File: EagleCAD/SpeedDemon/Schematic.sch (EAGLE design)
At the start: 45 parts, among them Q1 DMC2700, U1 LM3676, U3 STM32F072-LQFP48

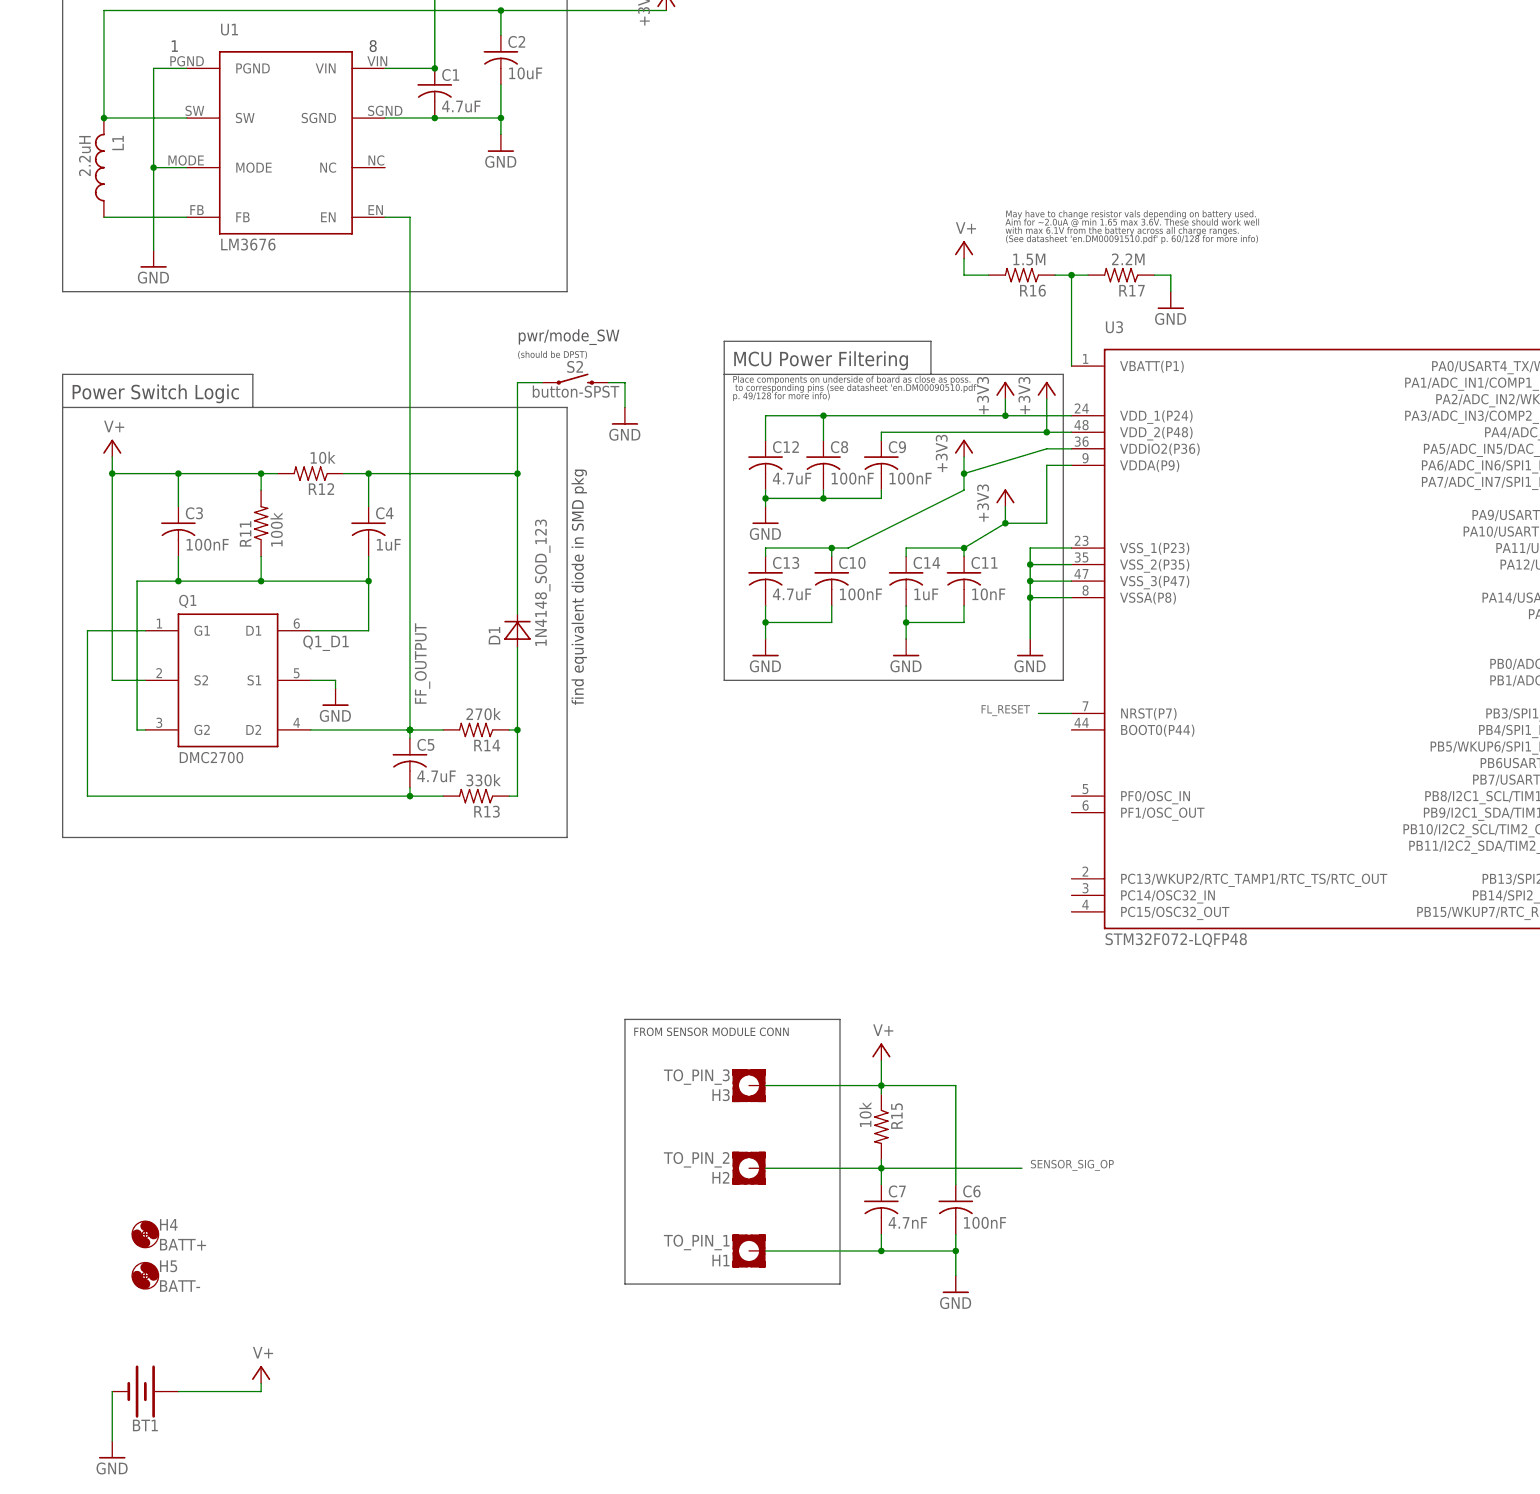
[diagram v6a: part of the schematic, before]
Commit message: Added thermal pad to switching regulator library part. Updated schematic.
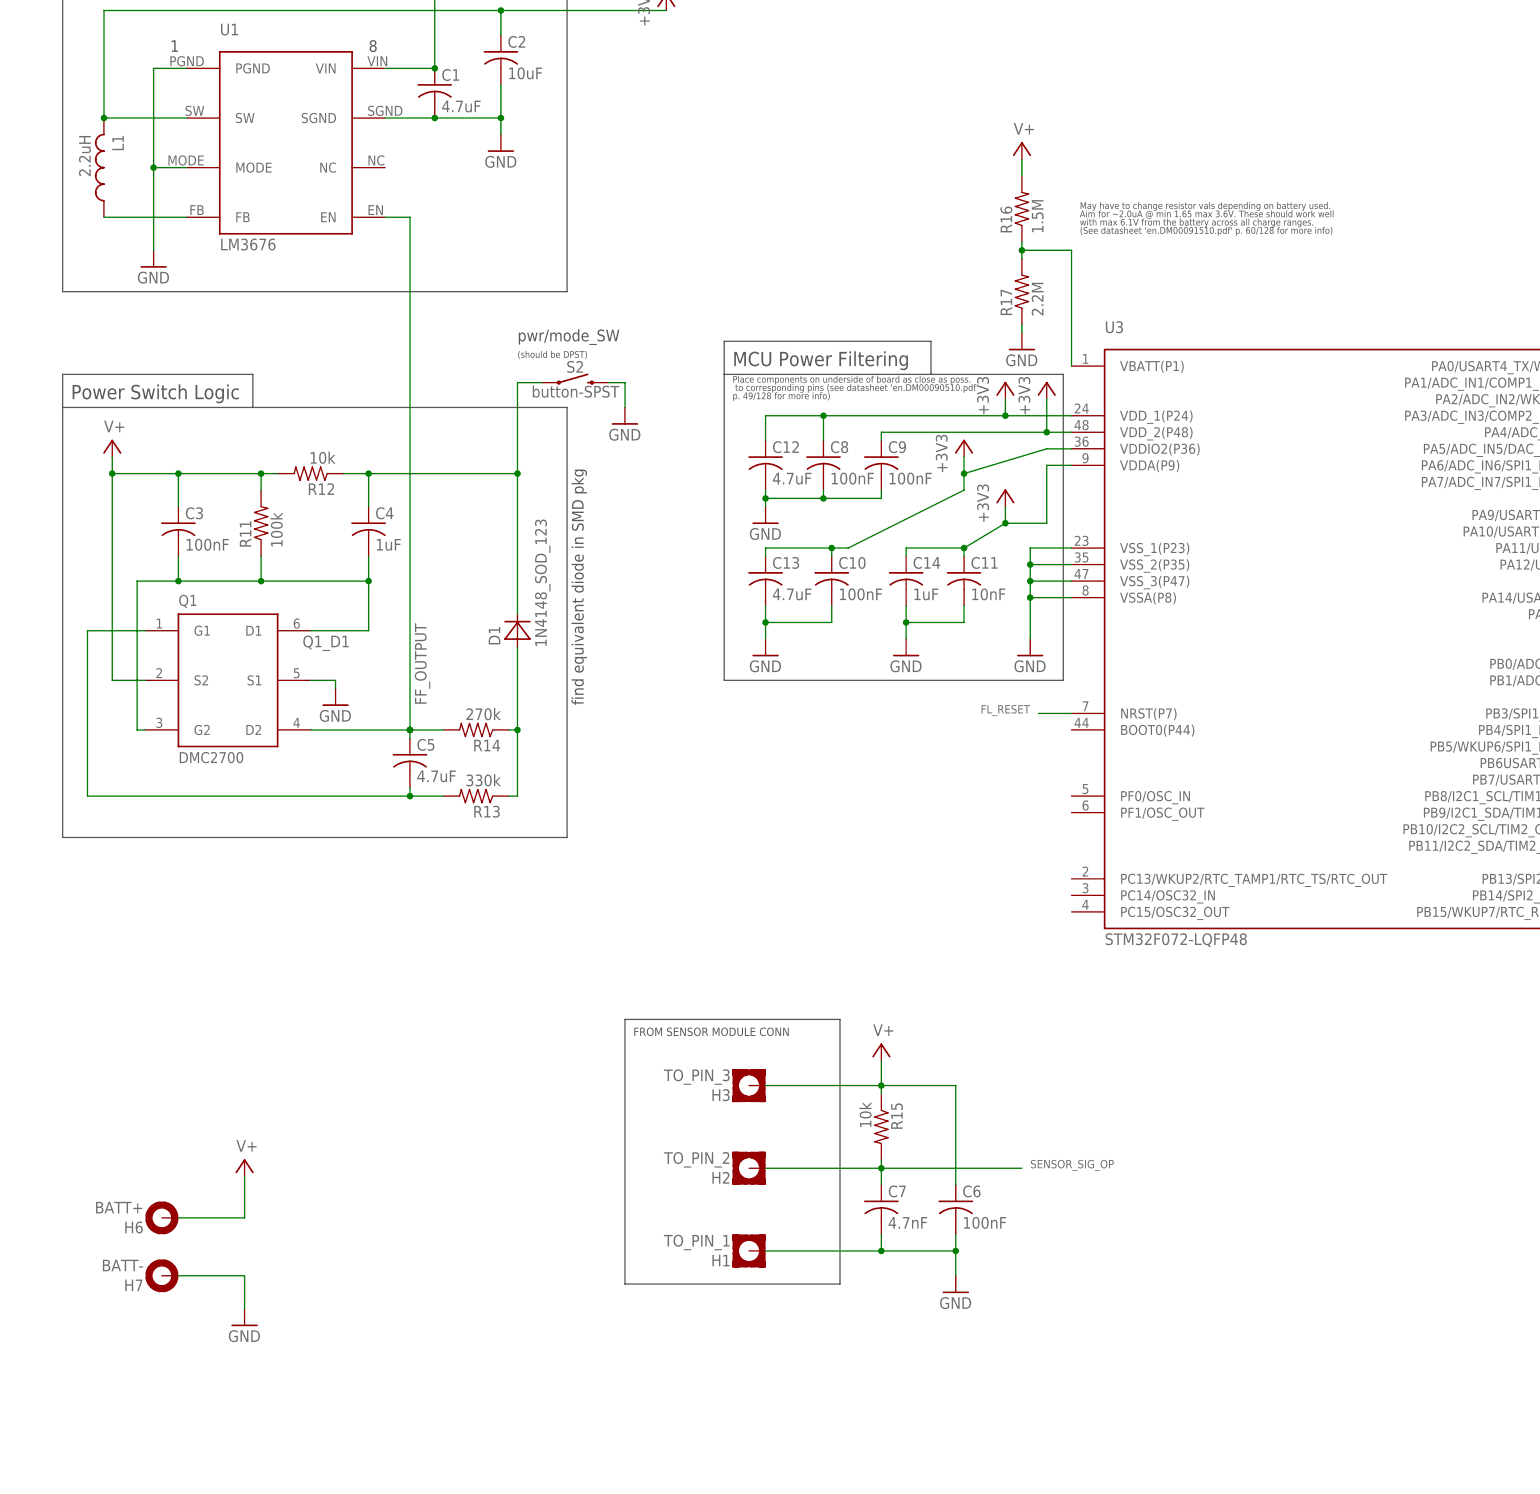
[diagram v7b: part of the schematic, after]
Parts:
- removed BT1: (no value), SparkFun-Batteries:BATTERY-9V
- removed H4: BATT+, holes:MOUNT-HOLE4.1
- removed H5: BATT-, holes:MOUNT-HOLE4.1
- added H6: BATT+, holes:MOUNT-PAD-ROUND3.6
- added H7: BATT-, holes:MOUNT-PAD-ROUND3.6
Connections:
- net GND: now also H7.MOUNT; no longer BT1.-
- net V+: now also H6.MOUNT; no longer BT1.+
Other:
- moved on the sheet: R16, R17

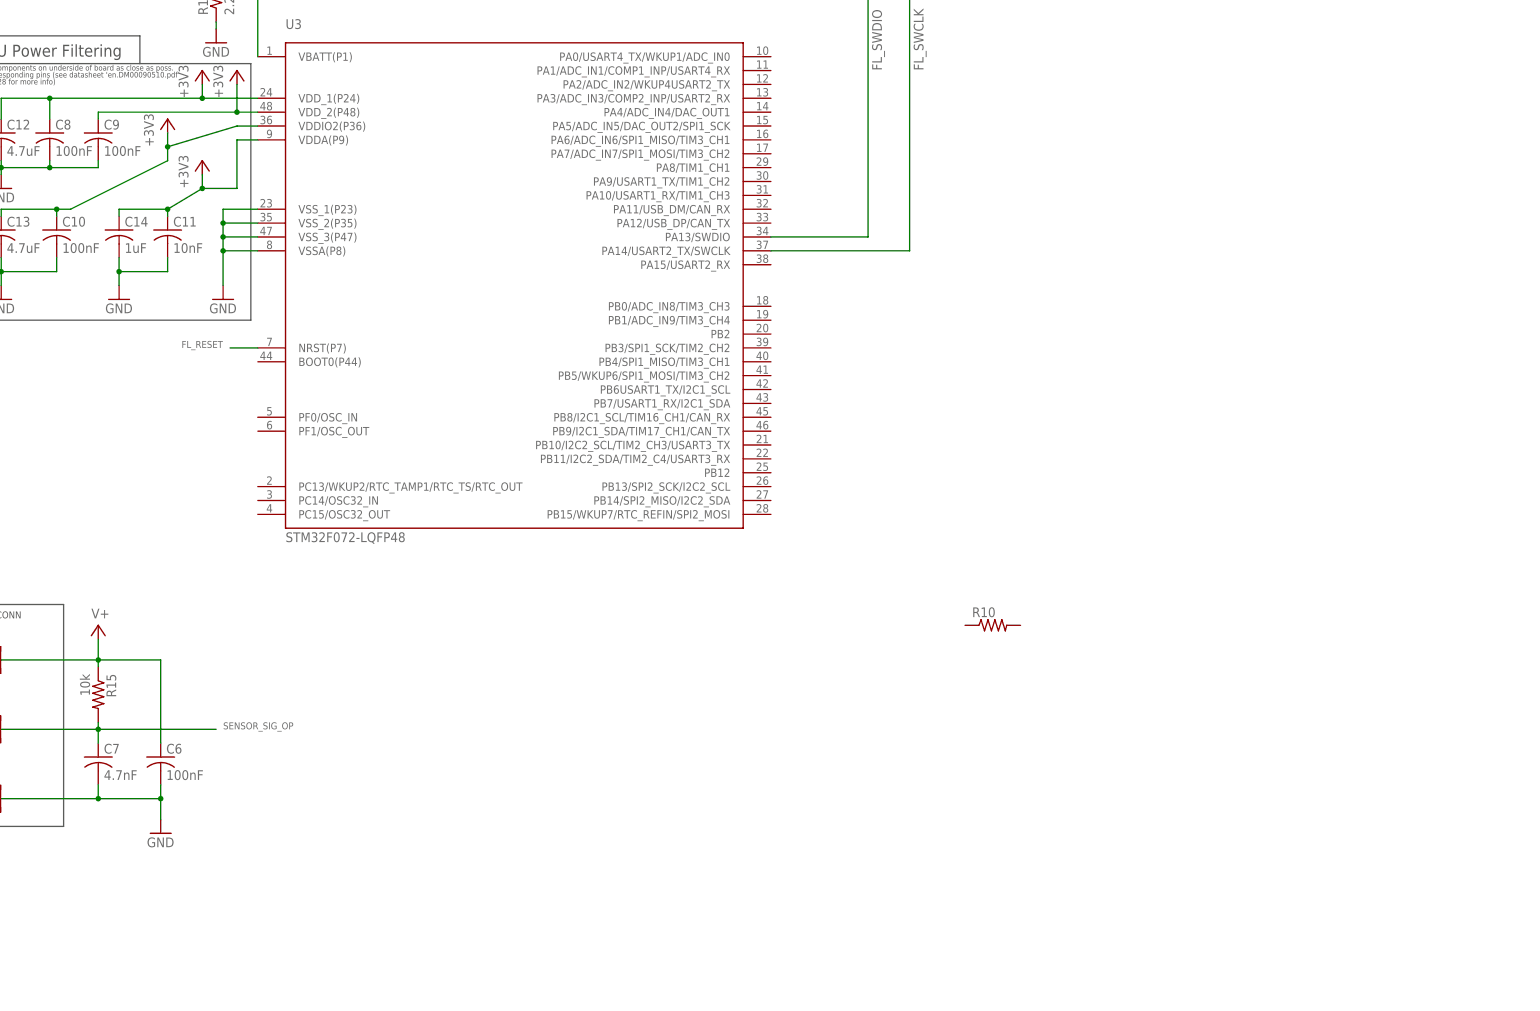
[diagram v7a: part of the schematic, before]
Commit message: Added LCD and 5-way button to schematic.
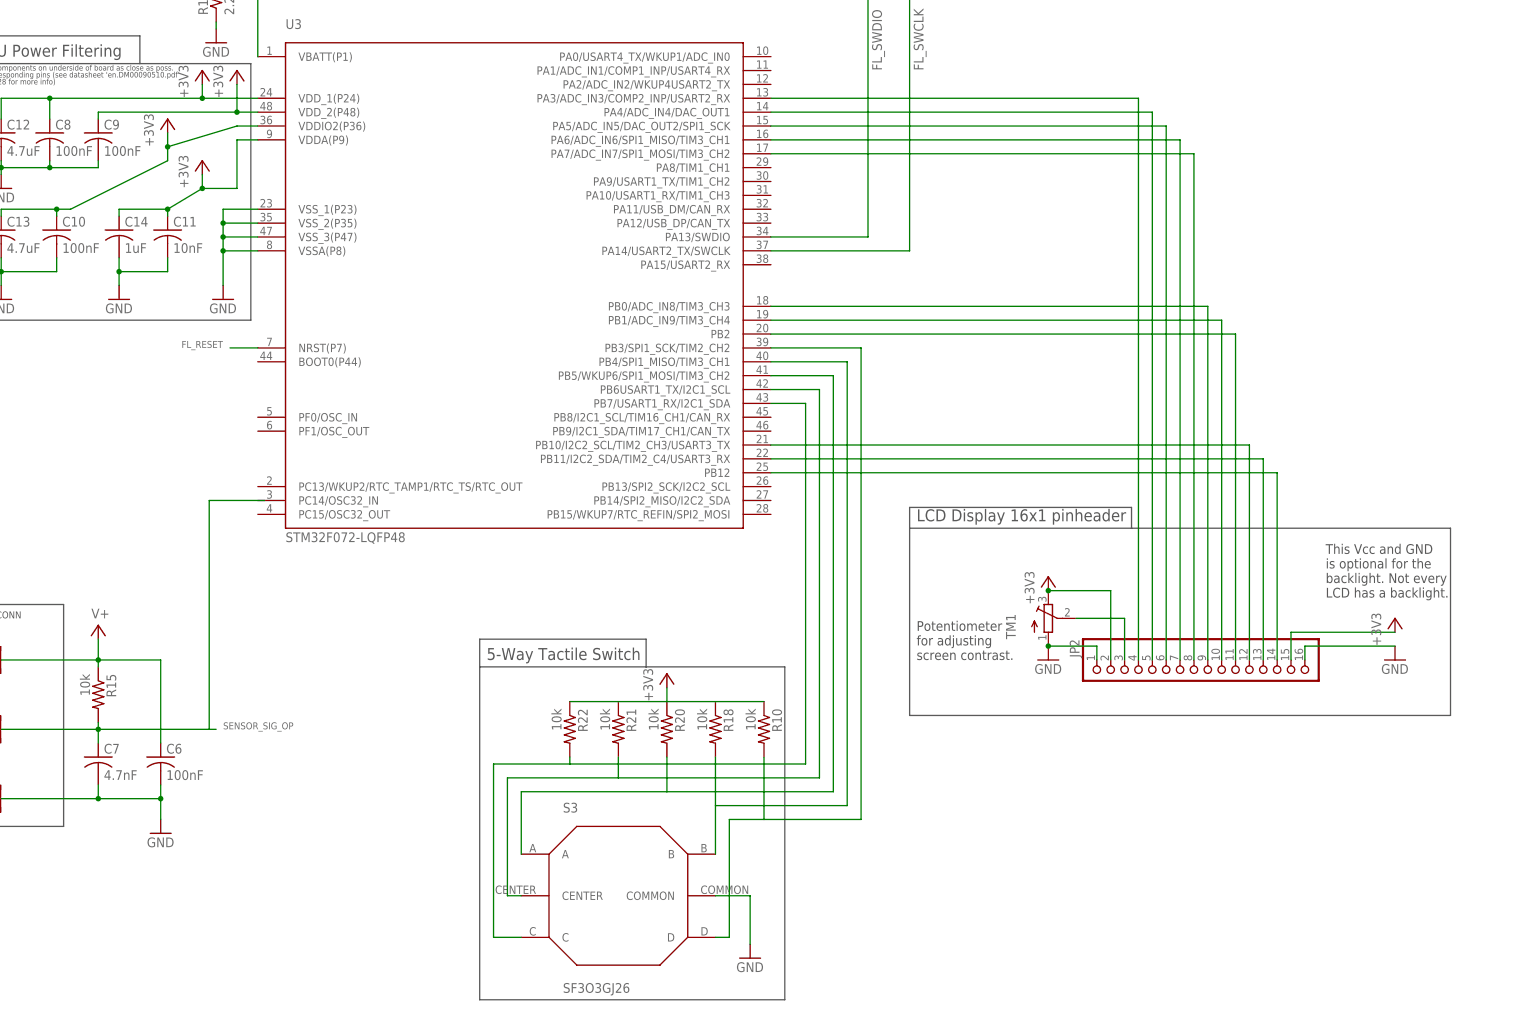
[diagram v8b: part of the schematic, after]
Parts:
- added JP2: (no value), pinhead:PINHD-1X16
- added R18, R20, R21, R22: 10k, 0805_generics:R_0805
- added S3: SF3O3GJ26, SF3O3GJ26:SF3O3GJ26
- added TM1: (no value), adafruit:TRIMPOT3386
- R10: value (none) -> 10k; device rcl:R-US_R0805 -> 0805_generics:R_0805
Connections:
- new net N$12: JP2.9, U3.PB0/ADC_IN8/TIM3_CH3
- new net N$13: JP2.10, U3.PB1/ADC_IN9/TIM3_CH4
- new net N$14: JP2.3, TM1.S
- new net N$16: JP2.4, U3.PA3/ADC_IN3/COMP2_INP/USART2_RX
- new net N$17: JP2.5, U3.PA4/ADC_IN4/DAC_OUT1
- new net N$18: JP2.6, U3.PA5/ADC_IN5/DAC_OUT2/SPI1_SCK
- new net N$19: JP2.7, U3.PA6/ADC_IN6/SPI1_MISO/TIM3_CH1
- new net N$20: JP2.8, U3.PA7/ADC_IN7/SPI1_MOSI/TIM3_CH2
- new net N$21: JP2.11, U3.PB2
- new net N$22: JP2.12, U3.PB10/I2C2_SCL/TIM2_CH3/USART3_TX
- new net N$23: JP2.13, U3.PB11/I2C2_SDA/TIM2_C4/USART3_RX
- new net N$24: JP2.14, U3.PB12
- new net N$25: R22.2, S3.C, U3.PB7/USART1_RX/I2C1_SDA
- new net N$26: R21.2, S3.CENTER, U3.PB6USART1_TX/I2C1_SCL
- new net N$27: R20.2, S3.A, U3.PB5/WKUP6/SPI1_MOSI/TIM3_CH2
- new net N$29: R18.2, S3.B, U3.PB4/SPI1_MISO/TIM3_CH1
- new net N$30: R10.2, S3.D, U3.PB3/SPI1_SCK/TIM2_CH2
- net +3V3: now also JP2.15, JP2.2, R10.1, R18.1, R20.1, R21.1, R22.1, TM1.E
- net GND: now also JP2.1, JP2.16, S3.COMMON, TM1.A
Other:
- note added: "5-Way Tactile Switch"
- note added: "LCD Display 16x1 pinheader"
- note added: "Potentiometer for adjusting screen contrast."
- note added: "This Vcc and GND is optional for the backlight. Not every LCD has a backlight."
- moved on the sheet: R10
